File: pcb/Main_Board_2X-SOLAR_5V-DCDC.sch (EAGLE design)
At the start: 97 parts, among them CN1 DCIN, CN5 USBA_FEMALE, CN6 MicroUSB, IC1 MCP73871, IC2 MCP73871, T2 MMUN2133LT1G, U3 TPS61090RSAR, U4 MCP73871

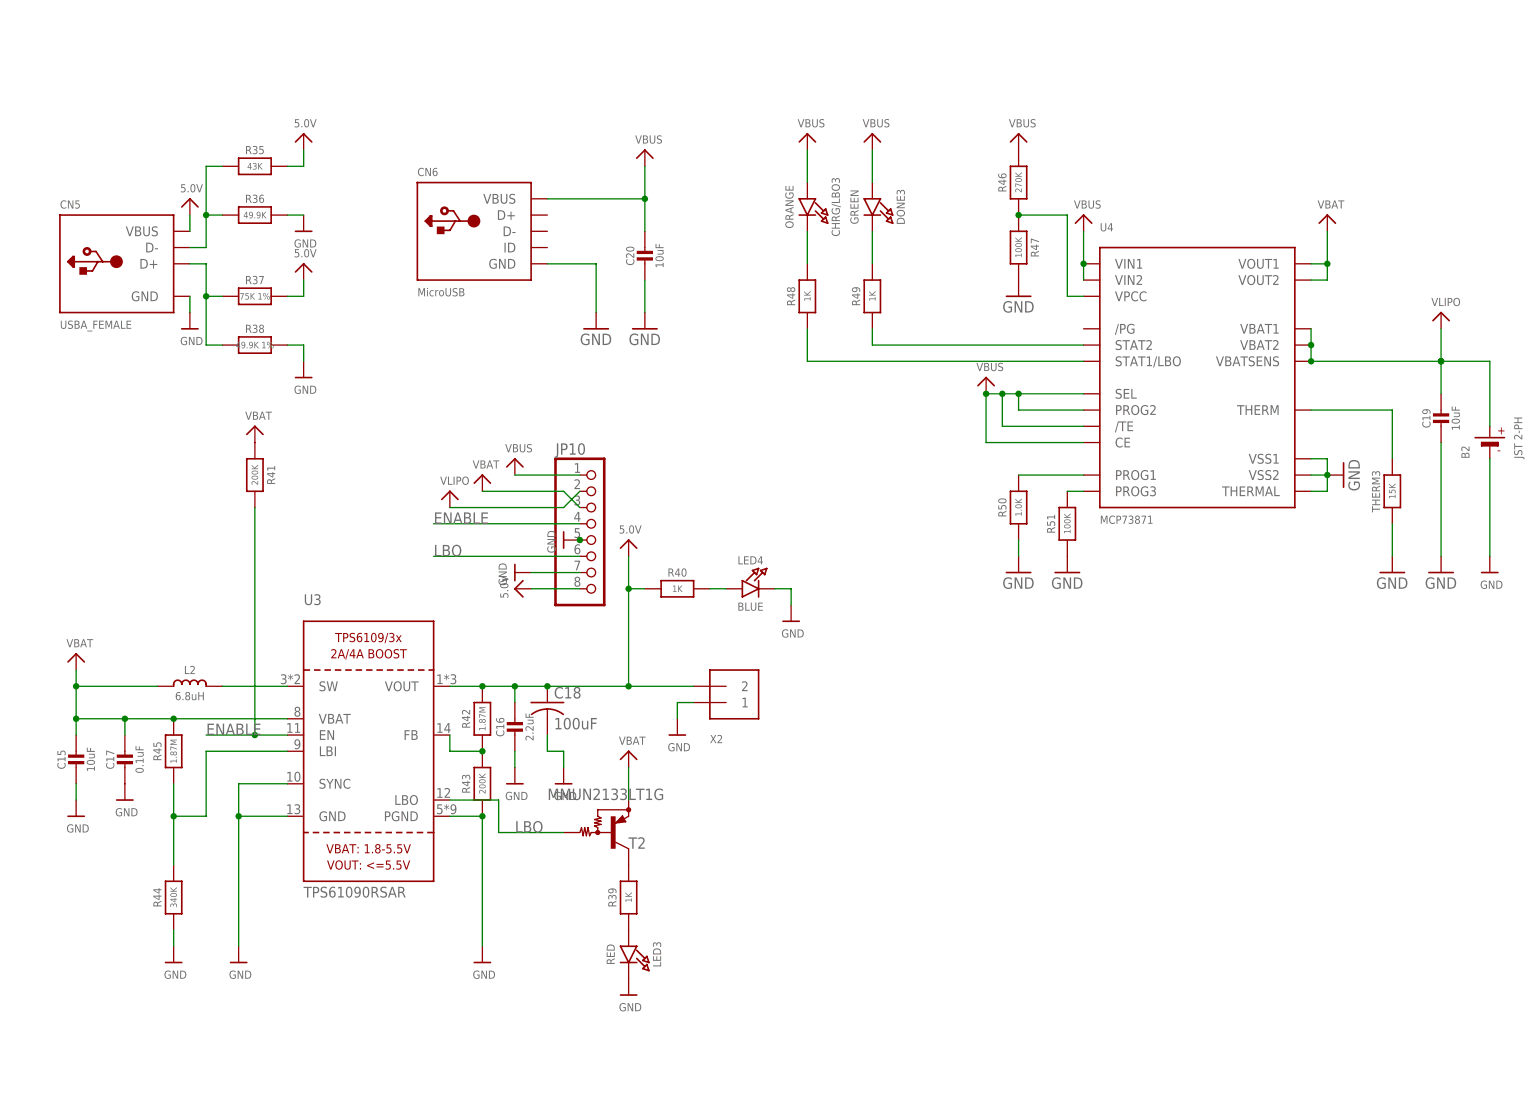
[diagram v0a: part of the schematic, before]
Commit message: Added 5V board and fixed PCB layout
Added 5V step up board loayout to main PCB. Removed additional MCP module from 5V layout.
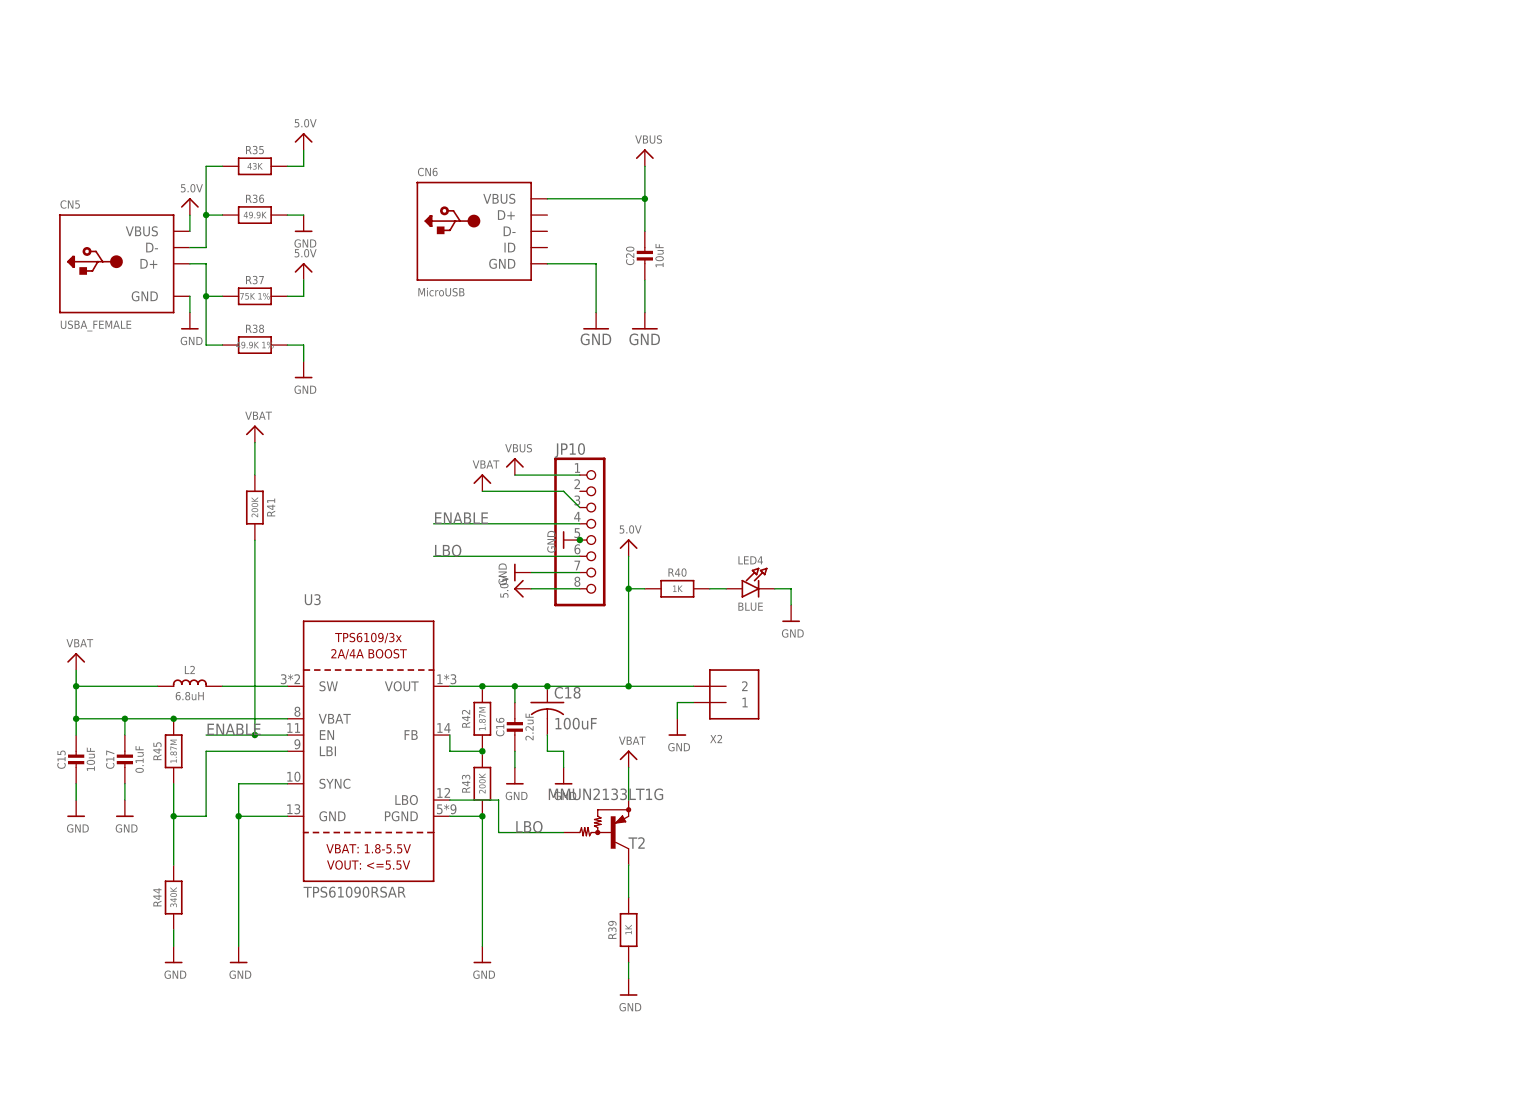
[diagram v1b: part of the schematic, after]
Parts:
- removed B2: JST 2-PH, microbuilder:BATTERY
- removed C19: 10uF, microbuilder:CAP_CERAMIC0805-NOOUTLINE
- removed CHRG/LBO3: ORANGE, microbuilder:LED0805_NOOUTLINE
- removed DONE3: GREEN, microbuilder:LED0805_NOOUTLINE
- removed LED3: RED, microbuilder:LED0805_NOOUTLINE
- removed R46: 270K, microbuilder:RESISTOR0805_NOOUTLINE
- removed R47, R51: 100K, microbuilder:RESISTOR0805_NOOUTLINE
- removed R48, R49: 1K, microbuilder:RESISTOR0805_NOOUTLINE
- removed R50: 1.0K, microbuilder:RESISTOR0805_NOOUTLINE
- removed THERM3: 15K, microbuilder:RESISTOR0805_NOOUTLINE
- removed U4: MCP73871, microbuilder:MCP73871
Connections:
- net N$3 renamed GNDBREAK
- removed net N$45: R46.1, R47.1, U4.VPCC
- removed net N$46: R49.1, U4.STAT2
- removed net N$47: R48.1, U4.STAT1/LBO
- removed net N$48: R50.2, U4.PROG1
- removed net N$49: THERM3.2, U4.THERM
- removed net N$50: DONE3.C, R49.2
- removed net N$51: CHRG/LBO3.C, R48.2
- removed net N$52: R51.2, U4.PROG3
- removed net VLIPO: B2.+, C19.1, JP10.2, U4.VBAT1, U4.VBAT2, U4.VBATSENS
- new net N$26: R39.2, T2.C
- net GND: now also C17.2, R39.1; no longer B2.-, C19.2, R50.1, THERM3.1, U4.THERMAL, U4.VSS1, U4.VSS2
- net VBAT: now also R41.1; no longer U4.VOUT1, U4.VOUT2
- net VBUS: no longer CHRG/LBO3.A, DONE3.A, U4./TE, U4.CE, U4.PROG2, U4.SEL, U4.VIN1, U4.VIN2
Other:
- moved on the sheet: R39, R41

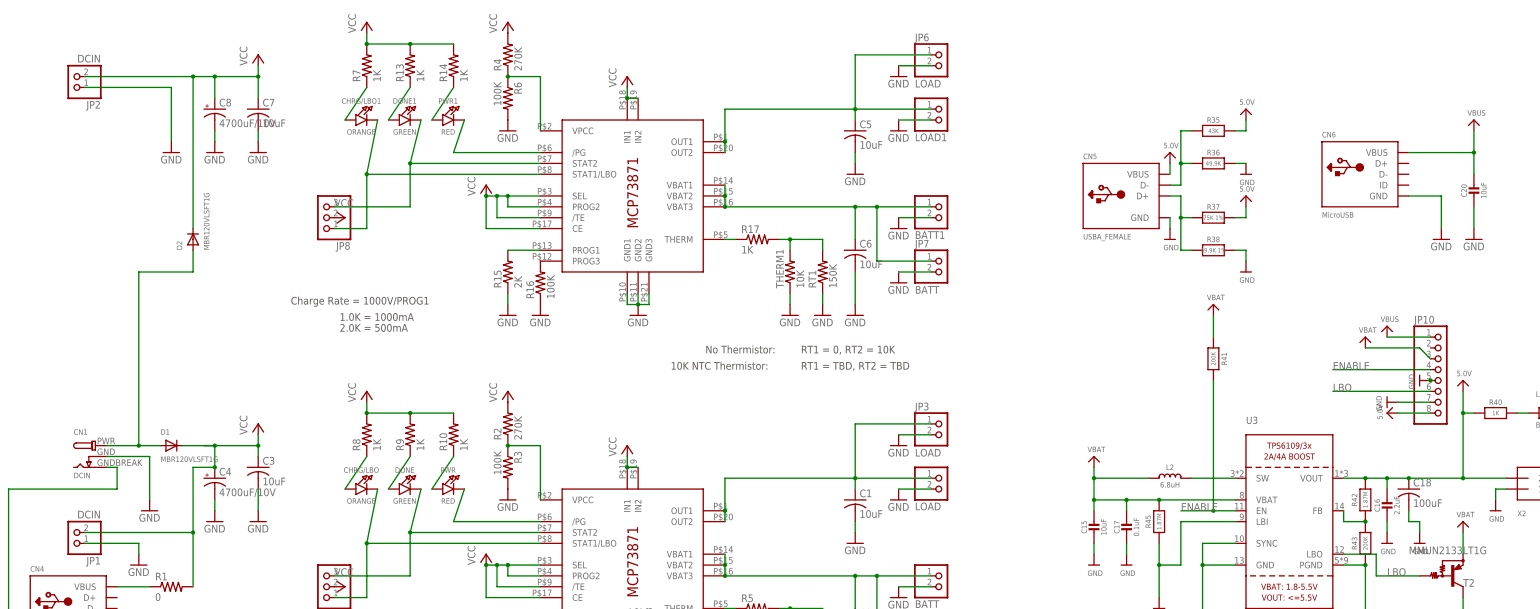
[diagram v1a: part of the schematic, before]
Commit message: Completed board layout
Completed layout for 2 MCP chips and TI 5V step-up boost. MCP load outputs merged and routed to 5V step-up, no 5V power wires needed. Added terminal block option for solar panel input. Added BOM folder and PCB quotes spreadsheet.
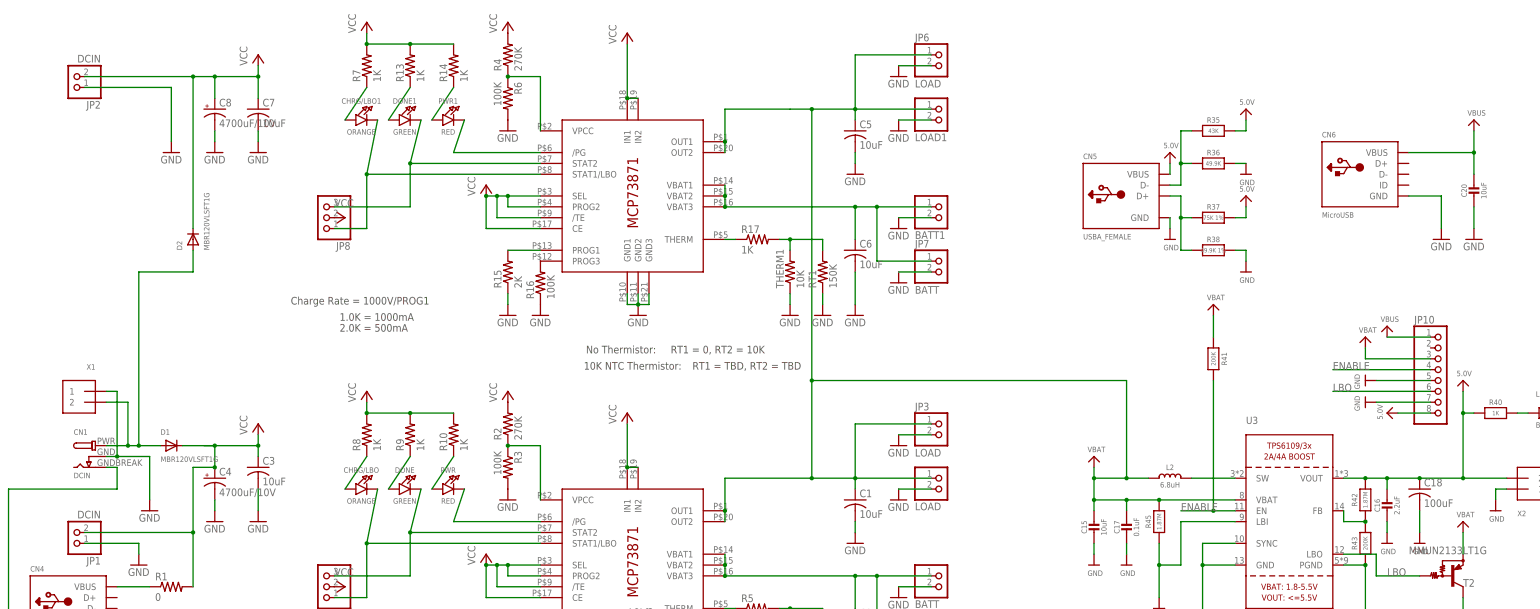
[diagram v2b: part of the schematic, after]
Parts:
- added X1: (no value), microbuilder:TERMBLOCK_1X2
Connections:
- net N$39 renamed SW
- net N$40 renamed LBI
- net N$6 renamed VPCC
- net N$7 renamed VPCC1
- removed net OUT: C1.1, IC1.OUT1, IC1.OUT2, JP3.1, LOAD.2
- removed net OUT1: C5.1, IC2.OUT1, IC2.OUT2, JP6.1, LOAD1.2
- net GND: now also X1.1
- net PV_IN: now also X1.2
- net VBAT: now also C1.1, C5.1, IC1.OUT1, IC1.OUT2, IC2.OUT1, IC2.OUT2, JP3.1, JP6.1, LOAD.2, LOAD1.2
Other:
- moved on the sheet: C18

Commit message: PCB board rev 1
Files used to print prototype from bayareacircuits. Adding BOM file and CAM/GERBER files
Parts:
- R11, R15: value 2K -> 1K
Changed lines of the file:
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@@
 <part name="GND6" library="supply1" deviceset="GND" device=""/>
 <part name="GND7" library="supply1" deviceset="GND" device=""/>
-<part name="R11" library="adafruit" deviceset="R-US_" device="FLIPFLOP" value="2K"/>
+<part name="R11" library="adafruit" deviceset="R-US_" device="FLIPFLOP" value="1K"/>
 <part name="R12" library="adafruit" deviceset="R-US_" device="R0805" value="100K"/>
 <part name="GND10" library="supply1" deviceset="GND" device=""/>
@@
 <part name="GND21" library="supply1" deviceset="GND" device=""/>
 <part name="GND22" library="supply1" deviceset="GND" device=""/>
-<part name="R15" library="adafruit" deviceset="R-US_" device="FLIPFLOP" value="2K"/>
+<part name="R15" library="adafruit" deviceset="R-US_" device="FLIPFLOP" value="1K"/>
 <part name="R16" library="adafruit" deviceset="R-US_" device="R0805" value="100K"/>
 <part name="GND23" library="supply1" deviceset="GND" device=""/>

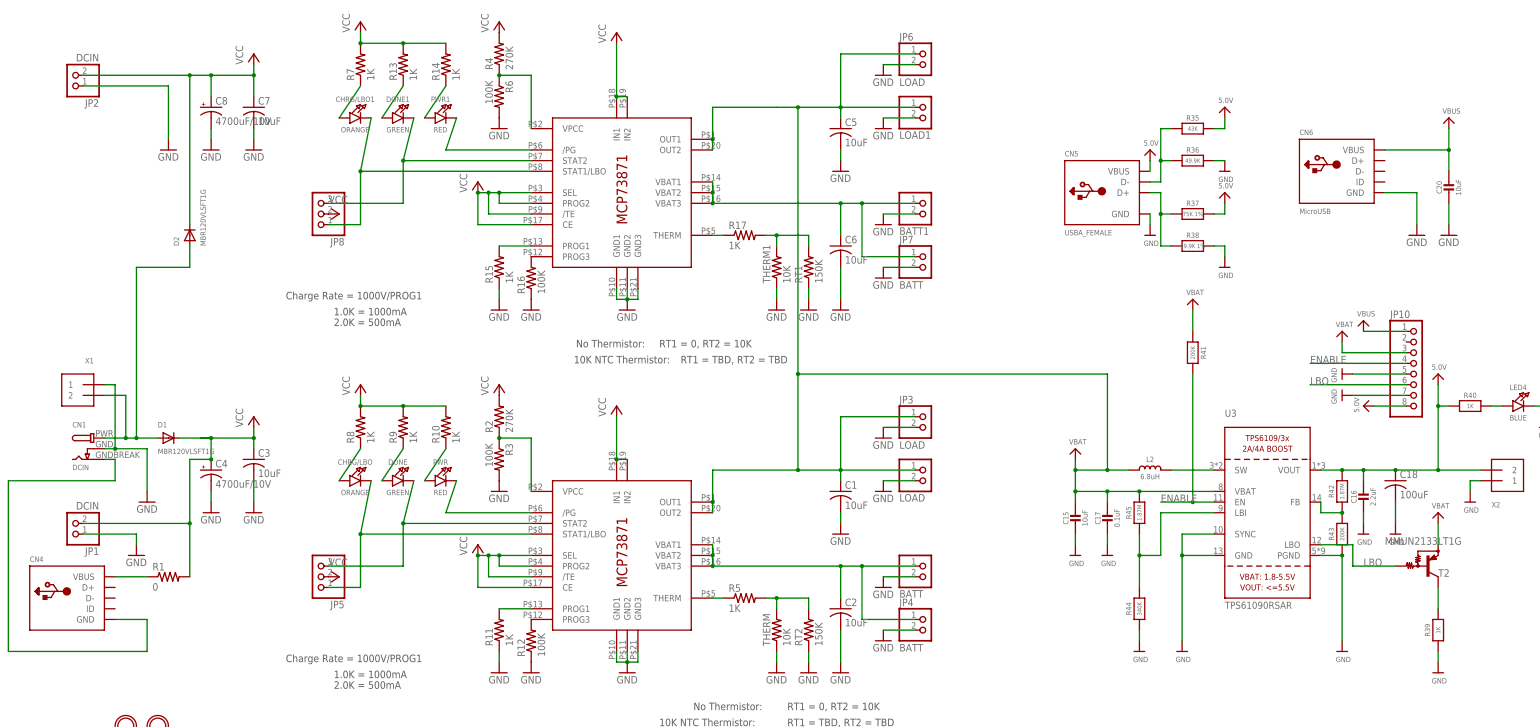
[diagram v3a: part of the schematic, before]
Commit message: Rev 2 start
Removed extra USB mounts, jumpers, and headers. BOM completed but missing a couple items from Digikey
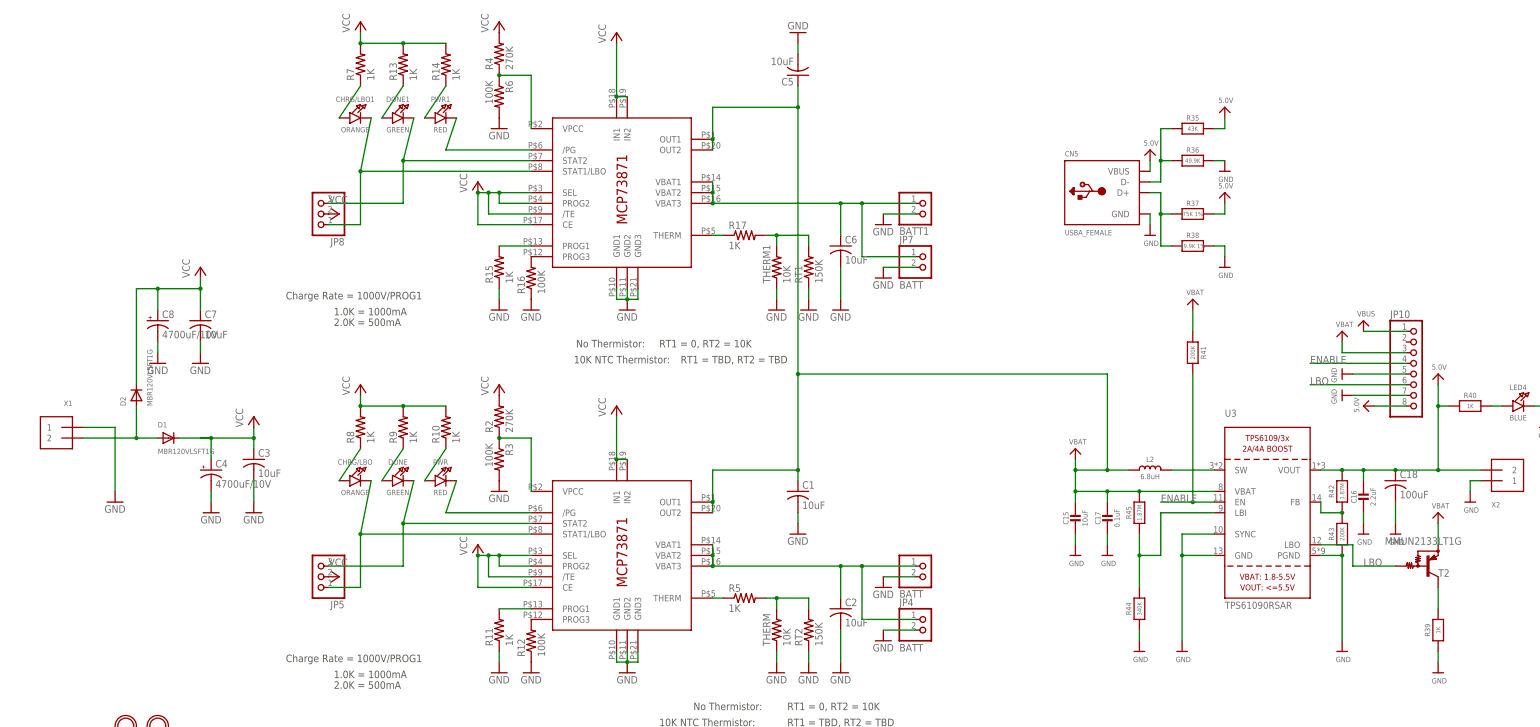
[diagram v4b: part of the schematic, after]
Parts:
- removed C20: 10uF, microbuilder:CAP_CERAMIC0805-NOOUTLINE
- removed CN1: DCIN, microbuilder:DCBARRELSMT
- removed CN4: (no value), microbuilder:USBMINIBLARGE
- removed CN6: MicroUSB, microbuilder:USBMICRO_20329
- removed JP1, JP2: DCIN, microbuilder:HEADER-1X2
- removed JP3, JP6: LOAD, microbuilder:HEADER-1X2ROUND
- removed LOAD, LOAD1: (no value), adafruit:JST_2PIN-SMT-RA
- removed R1: 0, adafruit:R-US_R0805
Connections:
- removed net GNDBREAK: CN1.GND, CN4.GND
- removed net N$2: CN4.VBUS, R1.1
- net GND: no longer C20.2, CN1.GNDBREAK, CN6.GND, JP1.1, JP2.1, JP3.2, JP6.2, LOAD.1, LOAD1.1
- net PV_IN: no longer CN1.PWR
- net VBAT: no longer JP3.1, JP6.1, LOAD.2, LOAD1.2
- net VBUS: no longer C20.1, CN6.VBUS
- net VCC: no longer JP1.2, JP2.2, R1.2
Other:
- moved on the sheet: C1, C5, C7, C8, D2, X1
